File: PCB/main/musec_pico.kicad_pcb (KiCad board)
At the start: 2 copper layers, 218 x 128.1 mm, 63 parts, among them J1 Pedal, J2 PJ313, J3 PJ313, SW1 SW_DIP_x01, SW2 SW_DIP_x01, SW3 SW_DIP_x01, SW4 SW_DIP_x01, SW5 SW_DIP_x01, SW6 SW_DIP_x01, SW7 SW_DIP_x01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

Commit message: PCB v1.22 for better PJ313 footprint
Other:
- board text added: "v1.22"
- board text removed: "v1.21"

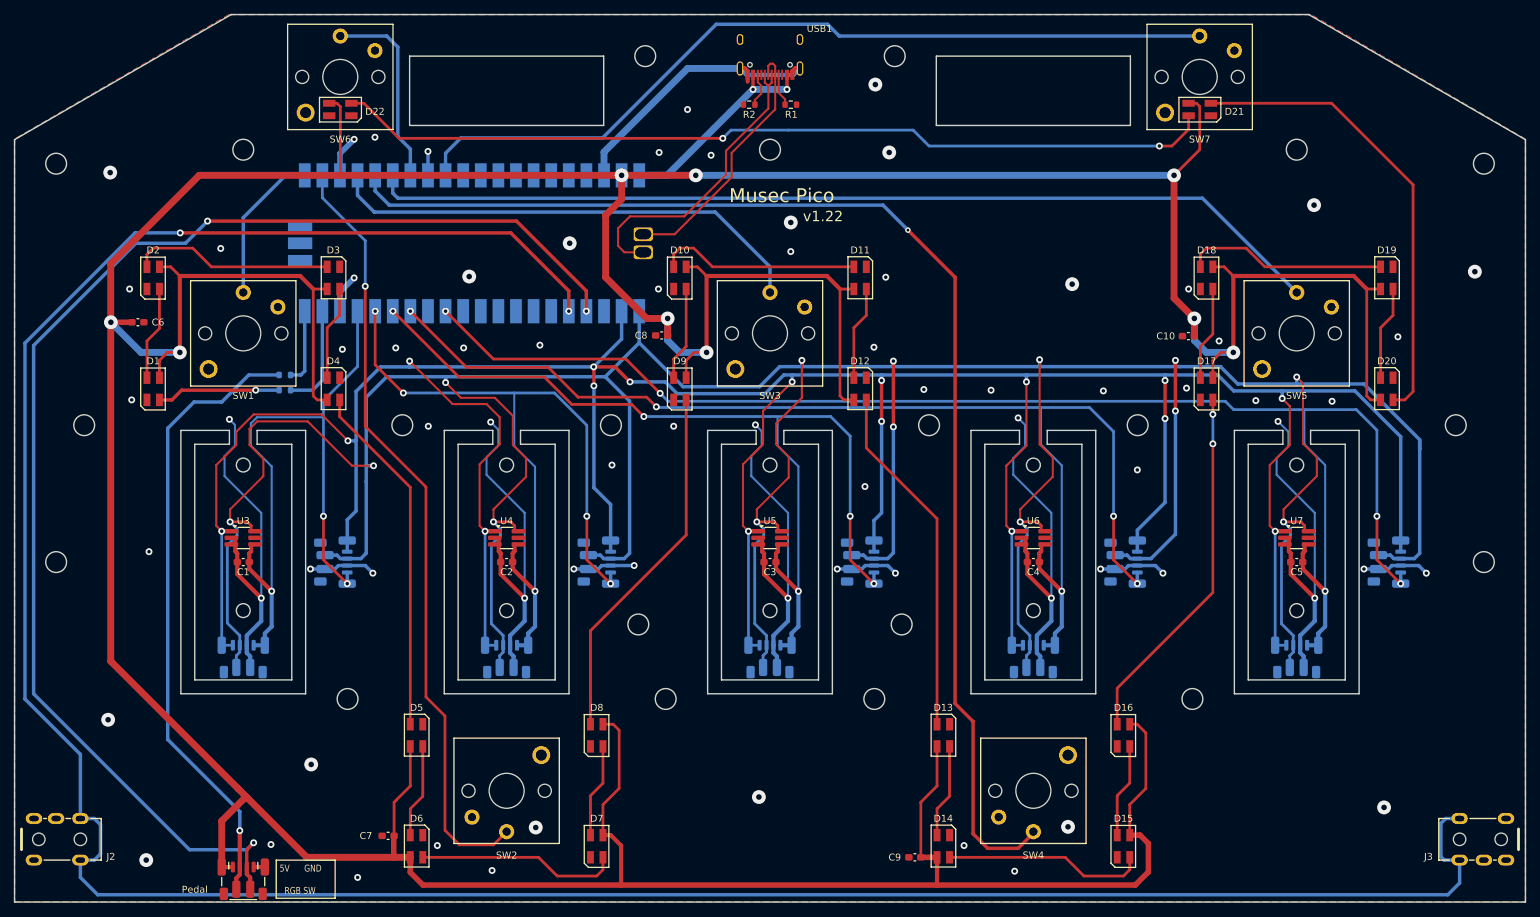
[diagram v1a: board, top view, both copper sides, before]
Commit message: PCB v1.23 better footprints
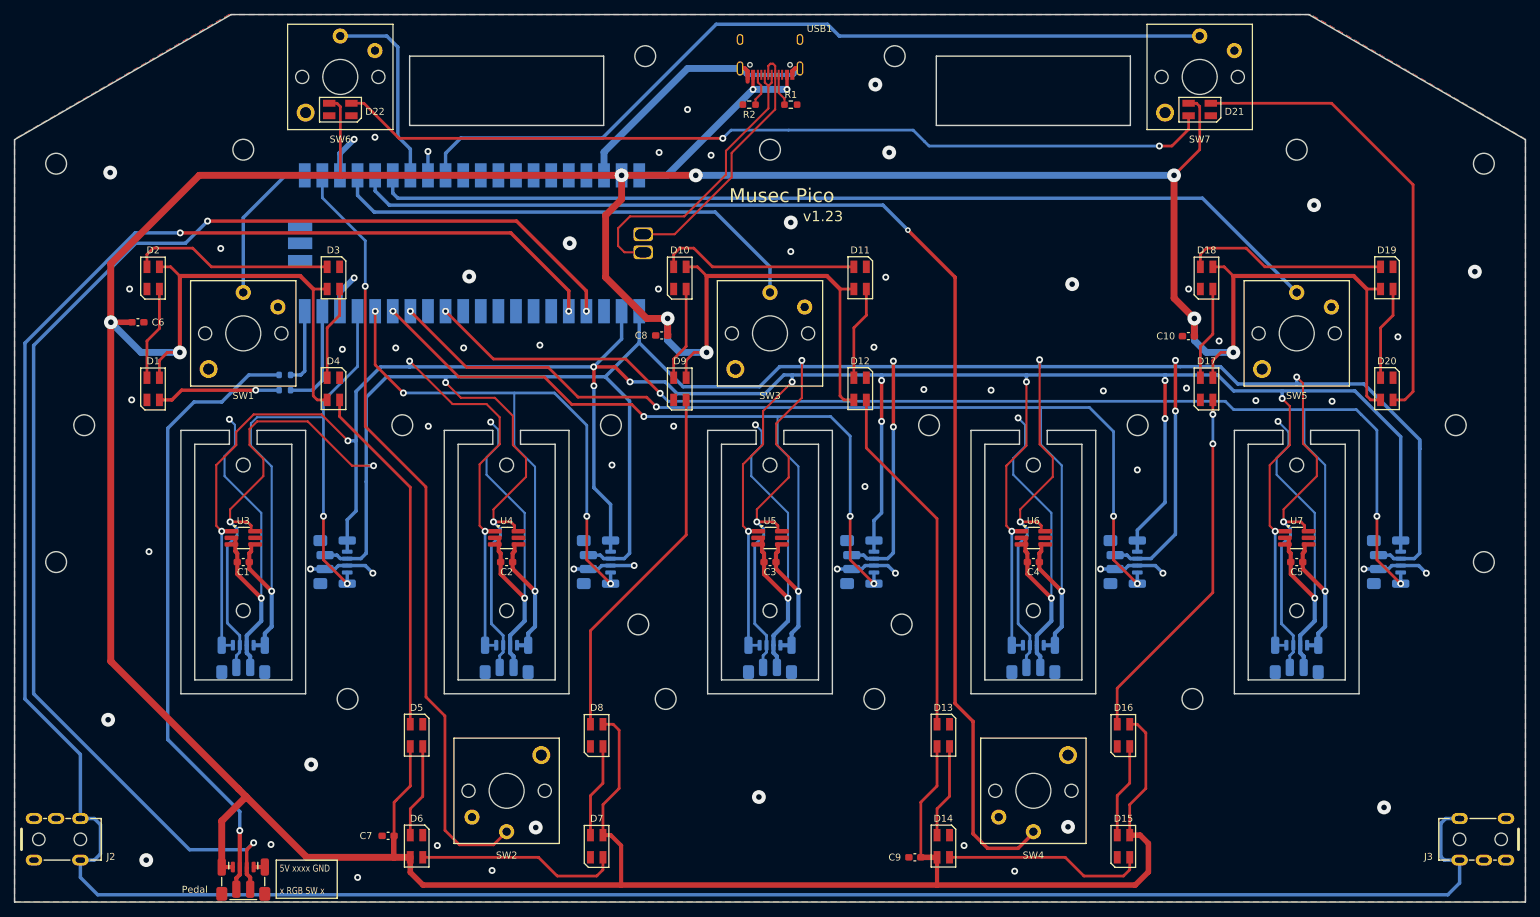
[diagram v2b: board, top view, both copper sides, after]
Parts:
- R1, R2: footprint Resistor_SMD:R_0603_1608Metric -> Resistor_SMD:R_0603_1608Metric_Pad0.98x0.95mm_HandSolder
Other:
- board text added: "5V xxxx GND x RGB SW x"
- board text added: "v1.23"
- board text removed: "5V GND RGB SW"
- board text removed: "v1.22"

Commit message: PCB v1.3 (a little bit easier soldering)
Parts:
- JA1, JA2, JA3, JA4, JA5: moved to F.Cu
- R3, R4: footprint Resistor_SMD:R_0603_1608Metric -> Resistor_SMD:R_0603_1608Metric_Pad0.98x0.95mm_HandSolder; moved to F.Cu
- moved R4 12.8 mm to (132.7, 123.7)
- moved R3 11.6 mm to (132.7, 121.7)
- turned JA1 to -90 degrees
- turned JA2 to -90 degrees
- turned JA3 to -90 degrees
- turned JA4 to -90 degrees
- turned JA5 to -90 degrees
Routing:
- net /SCL: track 532.6 -> 583.4 mm, vias 17 -> 22
- net /SDA: track 609.9 -> 628.2 mm, vias 14 -> 19
- net Net-(J1-Pin_2): track 90.3 -> 76.4 mm, vias 1 -> 2
- net Net-(U1-GPIO15): track 10.9 -> 23.9 mm, vias 0 -> 1
- net Net-(D1-In): track 17.9 -> 5.69 mm, vias 1 -> 0
- net Net-(U1-GPIO14): track 15.2 -> 25.4 mm, vias 0 -> 1
- net GND: track 356.8 -> 348.1 mm, vias 75 -> 87
- net /VB4: track 179.4 -> 173.2 mm, vias 5 -> 4
- net /VB5: track 212.1 -> 205.9 mm, vias 5 -> 4
- net /VB3: track 142.3 -> 136.0 mm, vias 5 -> 4
- net /VB2: track 115.6 -> 109.4 mm, vias 5 -> 4
- net /VB1: track 98.7 -> 92.5 mm, vias 3 -> 2
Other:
- board text added: "v1.3"
- board text removed: "v1.23"
